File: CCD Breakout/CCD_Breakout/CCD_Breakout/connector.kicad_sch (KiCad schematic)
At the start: 2 parts

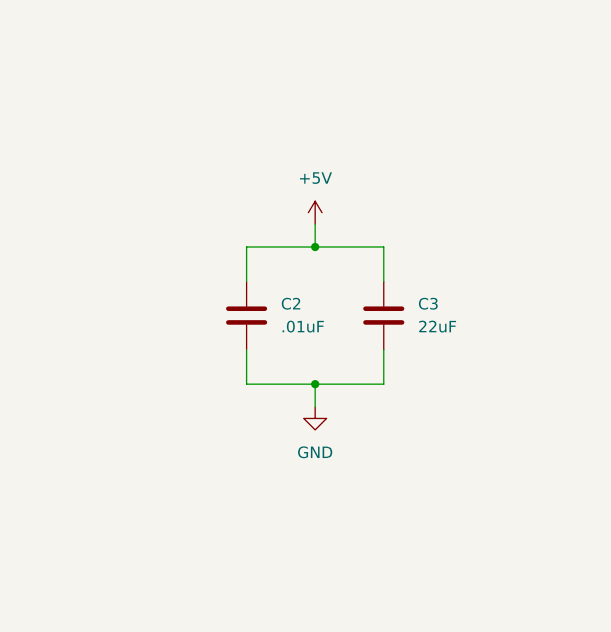
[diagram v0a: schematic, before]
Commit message: CCD Reorganization
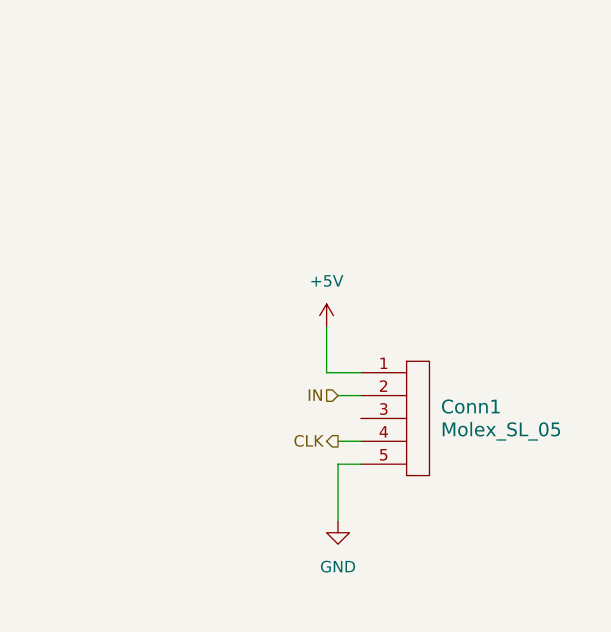
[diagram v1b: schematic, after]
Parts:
- removed C2: .01uF, symbol Device:C
- removed C3: 22uF, symbol Device:C
- added Conn1: Molex_SL_05, symbol MRDT_Connectors:Molex_SL_05
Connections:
- net +5V: now also Conn1.1
- net GND: now also Conn1.5
- new net CLK: Conn1.4
- new net IN: Conn1.2

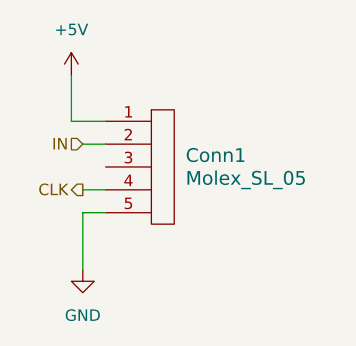
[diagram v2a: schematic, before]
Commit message: ADC Changes + Delete Fan Connector
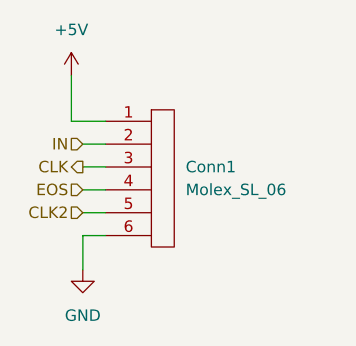
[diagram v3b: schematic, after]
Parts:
- removed Conn1: Molex_SL_05, symbol MRDT_Connectors:Molex_SL_05
- added Conn1: Molex_SL_06, symbol MRDT_Connectors:Molex_SL_06
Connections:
- net +5V: now also Conn1.1
- net CLK: now also Conn1.3
- net GND: now also Conn1.6
- net IN: now also Conn1.2
- new net CLK2: Conn1.5
- new net EOS: Conn1.4
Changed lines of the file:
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@@
+	(wire
+		(pts
+			(xy 149.86 97.79) (xy 152.4 97.79)
+		)
+		(stroke
+			(width 0)
+			(type default)
+		)
+	)
 	(wire
 		(pts
@@
 	(wire
 		(pts
-			(xy 149.86 97.79) (xy 152.4 97.79)
+			(xy 149.86 111.76) (xy 149.86 107.95)
 		)
 		(stroke
@@
 	(wire
 		(pts
-			(xy 149.86 111.76) (xy 149.86 105.41)
-		)
-		(stroke
-			(width 0)
-			(type default)
-		)
-	)
-	(wire
-		(pts
 			(xy 148.59 95.25) (xy 148.59 90.17)
 		)
@@
 	(wire
 		(pts
+			(xy 149.86 107.95) (xy 152.4 107.95)
+		)
+		(stroke
+			(width 0)
+			(type default)
+		)
+	)
+	(wire
+		(pts
 			(xy 152.4 95.25) (xy 148.59 95.25)
+		)
+		(stroke
+			(width 0)
+			(type default)
+		)
+	)
+	(wire
+		(pts
+			(xy 149.86 100.33) (xy 152.4 100.33)
 		)
 		(stroke
@@
 		)
 	)
-	(hierarchical_label "CLK"
-		(shape output)
+	(hierarchical_label "EOS"
+		(shape input)
 		(at 149.86 102.87 180)
 		(effects
@@
 		)
 	)
-	(symbol
-		(lib_id "MRDT_Connectors:Molex_SL_05")
-		(at 157.48 106.68 0)
-		(unit 1)
-		(exclude_from_sim no)
-		(in_bom yes)
-		(on_board yes)
-		(dnp no)
-		(fields_autoplaced yes)
-		(property "Reference" "Conn1"
-			(at 161.29 99.0599 0)
-			(effects
-				(font
-					(size 1.524 1.524)
-				)
-				(justify left)
-			)
-		)
-		(property "Value" "Molex_SL_05"
-			(at 161.29 101.5999 0)
-			(effects
-				(font
-					(size 1.524 1.524)
-				)
-				(justify left)
-			)
-		)
-		(property "Footprint" ""
-			(at 157.48 106.68 0)
-			(effects
-				(font
-					(size 1.524 1.524)
-				)
-				(hide yes)
-			)
-		)
-		(property "Datasheet" ""
-			(at 157.48 106.68 0)
-			(effects
-				(font
-					(size 1.524 1.524)
-				)
-				(hide yes)
-			)
-		)
-		(property "Description" ""
-			(at 157.48 106.68 0)
-			(effects
-				(font
-					(size 1.27 1.27)
-				)
-				(hide yes)
-			)
-		)
-		(pin "2"
-		)
-		(pin "1"
-		)
-		(pin "3"
-		)
-		(pin "5"
-		)
-		(pin "4"
-		)
-		(instances
-			(project ""
-				(path "/102965ac-29c6-4f96-94a4-d07431f6d693/dbede1ef-0855-4322-ae3b-1b9092ecc0c1"
-					(reference "Conn1")
-					(unit 1)
-				)
-			)
+	(hierarchical_label "CLK2"
+		(shape input)
+		(at 149.86 105.41 180)
+		(effects
+			(font
+				(size 1.27 1.27)
+			)
+			(justify right)
+		)
+	)
+	(hierarchical_label "CLK"
+		(shape output)
+		(at 149.86 100.33 180)
+		(effects
+			(font
+				(size 1.27 1.27)
+			)
+			(justify right)
 		)
 	)
@@
 					(unit 1)
 				)
+			)
+		)
+	)
+	(symbol
+		(lib_id "MRDT_Connectors:Molex_SL_06")
+		(at 157.48 109.22 0)
+		(unit 1)
+		(exclude_from_sim no)
+		(in_bom yes)
+		(on_board yes)
+		(dnp no)
+		(fields_autoplaced yes)
+		(property "Reference" "Conn1"
+			(at 161.29 100.3299 0)
+			(effects
+				(font
+					(size 1.27 1.27)
+				)
+				(justify left)
+			)
+		)
+		(property "Value" "Molex_SL_06"
+			(at 161.29 102.8699 0)
+			(effects
+				(font
+					(size 1.27 1.27)
+				)
+				(justify left)
+			)
+		)
+		(property "Footprint" ""
+			(at 152.4 105.41 0)
+			(effects
+				(font
+					(size 1.27 1.27)
+				)
+				(hide yes)
+			)
+		)
+		(property "Datasheet" ""
+			(at 152.4 105.41 0)
+			(effects
+				(font
+					(size 1.27 1.27)
+				)
+				(hide yes)
+			)
+		)
+		(property "Description" ""
+			(at 152.4 105.41 0)
+			(effects
+				(font
+					(size 1.27 1.27)
+				)
+				(hide yes)
+			)
+		)
+		(pin "1"
+		)
+		(pin "3"
+		)
+		(pin "5"
+		)
+		(pin "2"
+		)
+		(pin "4"
+		)
+		(pin "6"
+		)
+		(instances
+			(project ""
+				(path "/102965ac-29c6-4f96-94a4-d07431f6d693/dbede1ef-0855-4322-ae3b-1b9092ecc0c1"
+					(reference "Conn1")
+					(unit 1)
+				)

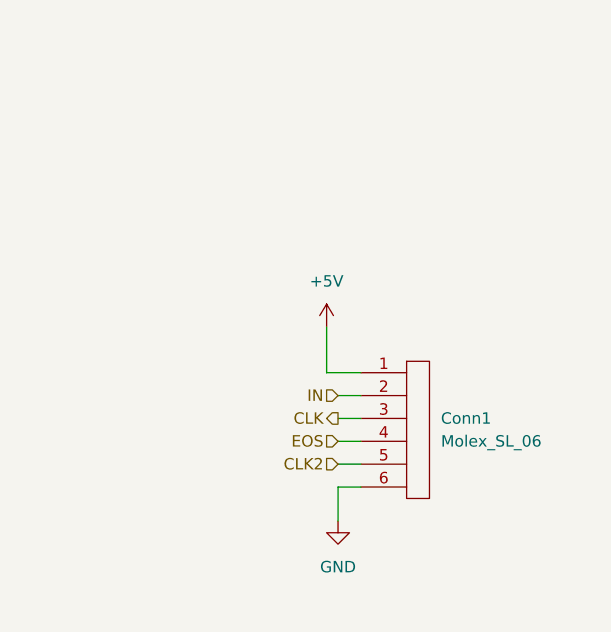
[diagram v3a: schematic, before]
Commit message: Removed Unnecessary Filtering Capacitors
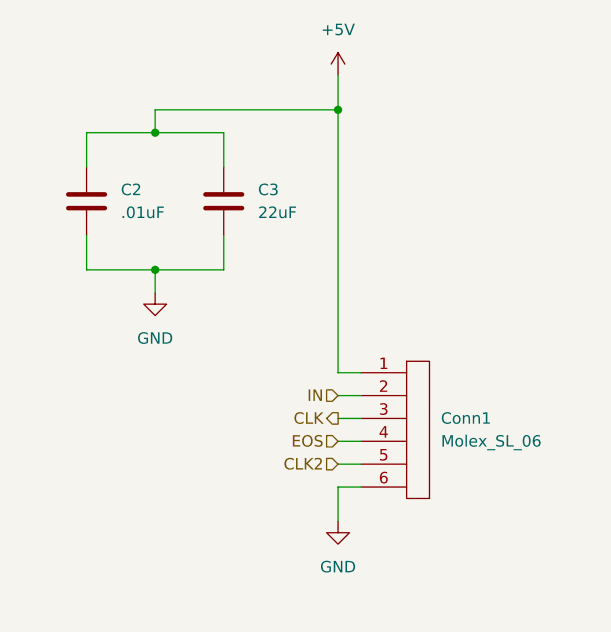
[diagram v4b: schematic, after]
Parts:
- added C2: .01uF, symbol Device:C
- added C3: 22uF, symbol Device:C
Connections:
- net +5V: now also C2.1, C3.1
- net GND: now also C2.2, C3.2

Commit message: ST and EOS Pin Connections
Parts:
- removed Conn1: Molex_SL_06, symbol MRDT_Connectors:Molex_SL_06
- added Conn1: Molex_SL_07, symbol MRDT_Connectors:Molex_SL_07
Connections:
- net +5V: now also Conn1.1
- net CLK: now also Conn1.3
- net CLK2: now also Conn1.6
- net EOS: now also Conn1.4
- net GND: now also Conn1.7
- net IN: now also Conn1.2
- new net ST: Conn1.5
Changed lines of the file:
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@@
+	(wire
+		(pts
+			(xy 152.4 110.49) (xy 149.86 110.49)
+		)
+		(stroke
+			(width 0)
+			(type default)
+		)
+	)
 	(wire
 		(pts
@@
 	(wire
 		(pts
+			(xy 149.86 110.49) (xy 149.86 115.57)
+		)
+		(stroke
+			(width 0)
+			(type default)
+		)
+	)
+	(wire
+		(pts
+			(xy 149.86 102.87) (xy 152.4 102.87)
+		)
+		(stroke
+			(width 0)
+			(type default)
+		)
+	)
+	(wire
+		(pts
+			(xy 149.86 62.23) (xy 149.86 66.04)
+		)
+		(stroke
+			(width 0)
+			(type default)
+		)
+	)
+	(wire
+		(pts
+			(xy 129.54 66.04) (xy 149.86 66.04)
+		)
+		(stroke
+			(width 0)
+			(type default)
+		)
+	)
+	(wire
+		(pts
+			(xy 152.4 95.25) (xy 149.86 95.25)
+		)
+		(stroke
+			(width 0)
+			(type default)
+		)
+	)
+	(wire
+		(pts
+			(xy 121.92 83.82) (xy 129.54 83.82)
+		)
+		(stroke
+			(width 0)
+			(type default)
+		)
+	)
+	(wire
+		(pts
+			(xy 149.86 107.95) (xy 152.4 107.95)
+		)
+		(stroke
+			(width 0)
+			(type default)
+		)
+	)
+	(wire
+		(pts
+			(xy 149.86 100.33) (xy 152.4 100.33)
+		)
+		(stroke
+			(width 0)
+			(type default)
+		)
+	)
+	(wire
+		(pts
+			(xy 121.92 80.01) (xy 121.92 83.82)
+		)
+		(stroke
+			(width 0)
+			(type default)
+		)
+	)
+	(wire
+		(pts
+			(xy 137.16 80.01) (xy 137.16 83.82)
+		)
+		(stroke
+			(width 0)
+			(type default)
+		)
+	)
+	(wire
+		(pts
 			(xy 149.86 105.41) (xy 152.4 105.41)
-		)
-		(stroke
-			(width 0)
-			(type default)
-		)
-	)
-	(wire
-		(pts
-			(xy 149.86 111.76) (xy 149.86 107.95)
-		)
-		(stroke
-			(width 0)
-			(type default)
-		)
-	)
-	(wire
-		(pts
-			(xy 149.86 102.87) (xy 152.4 102.87)
-		)
-		(stroke
-			(width 0)
-			(type default)
-		)
-	)
-	(wire
-		(pts
-			(xy 149.86 62.23) (xy 149.86 66.04)
-		)
-		(stroke
-			(width 0)
-			(type default)
-		)
-	)
-	(wire
-		(pts
-			(xy 129.54 66.04) (xy 149.86 66.04)
-		)
-		(stroke
-			(width 0)
-			(type default)
-		)
-	)
-	(wire
-		(pts
-			(xy 149.86 107.95) (xy 152.4 107.95)
-		)
-		(stroke
-			(width 0)
-			(type default)
-		)
-	)
-	(wire
-		(pts
-			(xy 152.4 95.25) (xy 149.86 95.25)
-		)
-		(stroke
-			(width 0)
-			(type default)
-		)
-	)
-	(wire
-		(pts
-			(xy 121.92 83.82) (xy 129.54 83.82)
-		)
-		(stroke
-			(width 0)
-			(type default)
-		)
-	)
-	(wire
-		(pts
-			(xy 149.86 100.33) (xy 152.4 100.33)
-		)
-		(stroke
-			(width 0)
-			(type default)
-		)
-	)
-	(wire
-		(pts
-			(xy 121.92 80.01) (xy 121.92 83.82)
-		)
-		(stroke
-			(width 0)
-			(type default)
-		)
-	)
-	(wire
-		(pts
-			(xy 137.16 80.01) (xy 137.16 83.82)
 		)
 		(stroke
@@
 		)
 	)
+	(hierarchical_label "ST"
+		(shape output)
+		(at 149.86 105.41 180)
+		(effects
+			(font
+				(size 1.27 1.27)
+			)
+			(justify right)
+		)
+	)
 	(hierarchical_label "EOS"
 		(shape input)
@@
 	(hierarchical_label "CLK2"
 		(shape input)
-		(at 149.86 105.41 180)
+		(at 149.86 107.95 180)
 		(effects
 			(font
@@
 	(symbol
 		(lib_id "power:GND")
-		(at 149.86 111.76 0)
+		(at 149.86 115.57 0)
 		(unit 1)
 		(exclude_from_sim no)
@@
 		(fields_autoplaced yes)
 		(property "Reference" "#PWR09"
-			(at 149.86 118.11 0)
+			(at 149.86 121.92 0)
 			(effects
 				(font
@@
 		)
 		(property "Value" "GND"
-			(at 149.86 116.84 0)
+			(at 149.86 120.65 0)
 			(effects
 				(font
@@
 		)
 		(property "Footprint" ""
-			(at 149.86 111.76 0)
+			(at 149.86 115.57 0)
 			(effects
 				(font
@@
 		)
 		(property "Datasheet" ""
-			(at 149.86 111.76 0)
+			(at 149.86 115.57 0)
 			(effects
 				(font
@@
 		)
 		(property "Description" "Power symbol creates a global label with name \"GND\" , ground"
-			(at 149.86 111.76 0)
+			(at 149.86 115.57 0)
 			(effects
 				(font
@@
 	)
 	(symbol
-		(lib_id "MRDT_Connectors:Molex_SL_06")
-		(at 157.48 109.22 0)
-		(unit 1)
-		(exclude_from_sim no)
-		(in_bom yes)
-		(on_board yes)
-		(dnp no)
-		(fields_autoplaced yes)
-		(property "Reference" "Conn1"
-			(at 161.29 100.3299 0)
-			(effects
-				(font
-					(size 1.27 1.27)
-				)
-				(justify left)
-			)
-		)
-		(property "Value" "Molex_SL_06"
-			(at 161.29 102.8699 0)
-			(effects
-				(font
-					(size 1.27 1.27)
-				)
-				(justify left)
-			)
-		)
-		(property "Footprint" ""
-			(at 152.4 105.41 0)
-			(effects
-				(font
-					(size 1.27 1.27)
-				)
-				(hide yes)
-			)
-		)
-		(property "Datasheet" ""
-			(at 152.4 105.41 0)
-			(effects
-				(font
-					(size 1.27 1.27)
-				)
-				(hide yes)
-			)
-		)
-		(property "Description" ""
-			(at 152.4 105.41 0)
-			(effects
-				(font
-					(size 1.27 1.27)
-				)
-				(hide yes)
-			)
-		)
-		(pin "1"
-		)
-		(pin "3"
-		)
-		(pin "5"
-		)
-		(pin "2"
-		)
-		(pin "4"
-		)
-		(pin "6"
-		)
-		(instances
-			(project ""
-				(path "/102965ac-29c6-4f96-94a4-d07431f6d693/dbede1ef-0855-4322-ae3b-1b9092ecc0c1"
-					(reference "Conn1")
-					(unit 1)
-				)
-			)
-		)
-	)
-	(symbol
 		(lib_id "power:GND")
 		(at 129.54 86.36 0)
@@
 					(unit 1)
 				)
+			)
+		)
+	)
+	(symbol
+		(lib_id "MRDT_Connectors:Molex_SL_07")
+		(at 157.48 111.76 0)
+		(unit 1)
+		(exclude_from_sim no)
+		(in_bom yes)
+		(on_board yes)
+		(dnp no)
+		(fields_autoplaced yes)
+		(property "Reference" "Conn1"
+			(at 161.29 101.5999 0)
+			(effects
+				(font
+					(size 1.524 1.524)
+				)
+				(justify left)
+			)
+		)
+		(property "Value" "Molex_SL_07"
+			(at 161.29 104.1399 0)
+			(effects
+				(font
+					(size 1.524 1.524)
+				)
+				(justify left)
+			)
+		)
+		(property "Footprint" ""
+			(at 157.48 106.68 0)
+			(effects
+				(font
+					(size 1.524 1.524)
+				)
+				(hide yes)
+			)
+		)
+		(property "Datasheet" ""
+			(at 157.48 106.68 0)
+			(effects
+				(font
+					(size 1.524 1.524)
+				)
+				(hide yes)
+			)
+		)
+		(property "Description" ""
+			(at 157.48 111.76 0)
+			(effects
+				(font
+					(size 1.27 1.27)
+				)
+				(hide yes)
+			)
+		)
+		(pin "5"
+		)
+		(pin "1"
+		)
+		(pin "3"
+		)
+		(pin "2"
+		)
+		(pin "4"
+		)
+		(pin "6"
+		)
+		(pin "7"
+		)
+		(instances
+			(project ""
+				(path "/102965ac-29c6-4f96-94a4-d07431f6d693/dbede1ef-0855-4322-ae3b-1b9092ecc0c1"
+					(reference "Conn1")
+					(unit 1)
+				)

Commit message: Fixed CCD Footprints
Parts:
- C2, C3: footprint (none) -> Capacitor_SMD:C_0603_1608Metric_Pad1.08x0.95mm_HandSolder
- Conn1: footprint (none) -> MRDT_Connectors:MOLEX_SL_07_Vertical
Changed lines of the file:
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@@
 			)
 		)
-		(property "Footprint" ""
+		(property "Footprint" "Capacitor_SMD:C_0603_1608Metric_Pad1.08x0.95mm_HandSolder"
 			(at 138.1252 80.01 0)
 			(effects
@@
 			)
 		)
-		(property "Footprint" ""
+		(property "Footprint" "MRDT_Connectors:MOLEX_SL_07_Vertical"
 			(at 157.48 106.68 0)
 			(effects
@@
 			)
 		)
-		(property "Footprint" ""
+		(property "Footprint" "Capacitor_SMD:C_0603_1608Metric_Pad1.08x0.95mm_HandSolder"
 			(at 122.8852 80.01 0)
 			(effects

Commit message: Added 3.3v to the CCD
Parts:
- removed Conn1: Molex_SL_07, MRDT_Connectors:MOLEX_SL_07_Vertical, symbol MRDT_Connectors:Molex_SL_07
- added Conn1: Molex_SL_08, symbol MRDT_Connectors:Molex_SL_08
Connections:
- net +5V: now also Conn1.2
- net CLK: now also Conn1.4
- net CLK2: now also Conn1.7
- net EOS: now also Conn1.5
- net GND: now also Conn1.8
- net IN: now also Conn1.3
- net ST: now also Conn1.6
- new net +3.3V: Conn1.1
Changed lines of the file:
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@@
 	(generator_version "9.0")
 	(paper "A4")
+	(text_box "Place this near to the connector"
+		(exclude_from_sim no)
+		(at 114.3 60.96 0)
+		(size 15.24 7.62)
+		(margins 0.9525 0.9525 0.9525 0.9525)
+		(stroke
+			(width 0)
+			(type solid)
+		)
+		(fill
+			(type none)
+		)
+		(effects
+			(font
+				(size 1.27 1.27)
+			)
+			(justify left top)
+		)
+	)
 	(junction
 		(at 149.86 66.04)
@@
 	(wire
 		(pts
+			(xy 147.32 92.71) (xy 152.4 92.71)
+		)
+		(stroke
+			(width 0)
+			(type default)
+		)
+	)
+	(wire
+		(pts
 			(xy 121.92 72.39) (xy 121.92 68.58)
 		)
@@
 		(pts
 			(xy 152.4 110.49) (xy 149.86 110.49)
+		)
+		(stroke
+			(width 0)
+			(type default)
+		)
+	)
+	(wire
+		(pts
+			(xy 147.32 87.63) (xy 147.32 92.71)
 		)
 		(stroke
@@
 	)
 	(symbol
+		(lib_id "power:+3.3V")
+		(at 147.32 87.63 0)
+		(unit 1)
+		(exclude_from_sim no)
+		(in_bom yes)
+		(on_board yes)
+		(dnp no)
+		(fields_autoplaced yes)
+		(property "Reference" "#PWR019"
+			(at 147.32 91.44 0)
+			(effects
+				(font
+					(size 1.27 1.27)
+				)
+				(hide yes)
+			)
+		)
+		(property "Value" "+3.3V"
+			(at 147.32 82.55 0)
+			(effects
+				(font
+					(size 1.27 1.27)
+				)
+			)
+		)
+		(property "Footprint" ""
+			(at 147.32 87.63 0)
+			(effects
+				(font
+					(size 1.27 1.27)
+				)
+				(hide yes)
+			)
+		)
+		(property "Datasheet" ""
+			(at 147.32 87.63 0)
+			(effects
+				(font
+					(size 1.27 1.27)
+				)
+				(hide yes)
+			)
+		)
+		(property "Description" "Power symbol creates a global label with name \"+3.3V\""
+			(at 147.32 87.63 0)
+			(effects
+				(font
+					(size 1.27 1.27)
+				)
+				(hide yes)
+			)
+		)
+		(pin "1"
+		)
+		(instances
+			(project ""
+				(path "/102965ac-29c6-4f96-94a4-d07431f6d693/dbede1ef-0855-4322-ae3b-1b9092ecc0c1"
+					(reference "#PWR019")
+					(unit 1)
+				)
+			)
+		)
+	)
+	(symbol
+		(lib_id "MRDT_Connectors:Molex_SL_08")
+		(at 157.48 111.76 0)
+		(unit 1)
+		(exclude_from_sim no)
+		(in_bom yes)
+		(on_board yes)
+		(dnp no)
+		(fields_autoplaced yes)
+		(property "Reference" "Conn1"
+			(at 161.29 100.3299 0)
+			(effects
+				(font
+					(size 1.524 1.524)
+				)
+				(justify left)
+			)
+		)
+		(property "Value" "Molex_SL_08"
+			(at 161.29 102.8699 0)
+			(effects
+				(font
+					(size 1.524 1.524)
+				)
+				(justify left)
+			)
+		)
+		(property "Footprint" ""
+			(at 157.48 104.14 0)
+			(effects
+				(font
+					(size 1.524 1.524)
+				)
+				(hide yes)
+			)
+		)
+		(property "Datasheet" ""
+			(at 157.48 104.14 0)
+			(effects
+				(font
+					(size 1.524 1.524)
+				)
+				(hide yes)
+			)
+		)
+		(property "Description" ""
+			(at 157.48 111.76 0)
+			(effects
+				(font
+					(size 1.27 1.27)
+				)
+				(hide yes)
+			)
+		)
+		(pin "2"
+		)
+		(pin "6"
+		)
+		(pin "5"
+		)
+		(pin "1"
+		)
+		(pin "8"
+		)
+		(pin "4"
+		)
+		(pin "7"
+		)
+		(pin "3"
+		)
+		(instances
+			(project ""
+				(path "/102965ac-29c6-4f96-94a4-d07431f6d693/dbede1ef-0855-4322-ae3b-1b9092ecc0c1"
+					(reference "Conn1")
+					(unit 1)
+				)
+			)
+		)
+	)
+	(symbol
 		(lib_id "power:GND")
 		(at 129.54 86.36 0)
@@
 					(unit 1)
 				)
-			)
-		)
-	)
-	(symbol
-		(lib_id "MRDT_Connectors:Molex_SL_07")
-		(at 157.48 111.76 0)
-		(unit 1)
-		(exclude_from_sim no)
-		(in_bom yes)
-		(on_board yes)
-		(dnp no)
-		(fields_autoplaced yes)
-		(property "Reference" "Conn1"
-			(at 161.29 101.5999 0)
-			(effects
-				(font
-					(size 1.524 1.524)
-				)
-				(justify left)
-			)
-		)
-		(property "Value" "Molex_SL_07"
-			(at 161.29 104.1399 0)
-			(effects
-				(font
-					(size 1.524 1.524)
-				)
-				(justify left)
-			)
-		)
-		(property "Footprint" "MRDT_Connectors:MOLEX_SL_07_Vertical"
-			(at 157.48 106.68 0)
-			(effects
-				(font
-					(size 1.524 1.524)
-				)
-				(hide yes)
-			)
-		)
-		(property "Datasheet" ""
-			(at 157.48 106.68 0)
-			(effects
-				(font
-					(size 1.524 1.524)
-				)
-				(hide yes)
-			)
-		)
-		(property "Description" ""
-			(at 157.48 111.76 0)
-			(effects
-				(font
-					(size 1.27 1.27)
-				)
-				(hide yes)
-			)
-		)
-		(pin "5"
-		)
-		(pin "1"
-		)
-		(pin "3"
-		)
-		(pin "2"
-		)
-		(pin "4"
-		)
-		(pin "6"
-		)
-		(pin "7"
-		)
-		(instances
-			(project ""
-				(path "/102965ac-29c6-4f96-94a4-d07431f6d693/dbede1ef-0855-4322-ae3b-1b9092ecc0c1"
-					(reference "Conn1")
-					(unit 1)
-				)

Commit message: Added 3.3v to ADC
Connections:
- net +3.3V renamed +3V3
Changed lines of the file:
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@@
+	)
+	(symbol
+		(lib_id "power:+3V3")
+		(at 147.32 87.63 0)
+		(unit 1)
+		(exclude_from_sim no)
+		(in_bom yes)
+		(on_board yes)
+		(dnp no)
+		(fields_autoplaced yes)
+		(property "Reference" "#PWR019"
+			(at 147.32 91.44 0)
+			(effects
+				(font
+					(size 1.27 1.27)
+				)
+				(hide yes)
+			)
+		)
+		(property "Value" "+3V3"
+			(at 147.32 82.55 0)
+			(effects
+				(font
+					(size 1.27 1.27)
+				)
+			)
+		)
+		(property "Footprint" ""
+			(at 147.32 87.63 0)
+			(effects
+				(font
+					(size 1.27 1.27)
+				)
+				(hide yes)
+			)
+		)
+		(property "Datasheet" ""
+			(at 147.32 87.63 0)
+			(effects
+				(font
+					(size 1.27 1.27)
+				)
+				(hide yes)
+			)
+		)
+		(property "Description" "Power symbol creates a global label with name \"+3V3\""
+			(at 147.32 87.63 0)
+			(effects
+				(font
+					(size 1.27 1.27)
+				)
+				(hide yes)
+			)
+		)
+		(pin "1"
+		)
+		(instances
+			(project ""
+				(path "/102965ac-29c6-4f96-94a4-d07431f6d693/dbede1ef-0855-4322-ae3b-1b9092ecc0c1"
+					(reference "#PWR019")
+					(unit 1)
+				)
+			)
+		)
 	)
 	(symbol
@@
 					(unit 1)
 				)
-			)
-		)
-	)
-	(symbol
-		(lib_id "power:+3.3V")
-		(at 147.32 87.63 0)
-		(unit 1)
-		(exclude_from_sim no)
-		(in_bom yes)
-		(on_board yes)
-		(dnp no)
-		(fields_autoplaced yes)
-		(property "Reference" "#PWR019"
-			(at 147.32 91.44 0)
-			(effects
-				(font
-					(size 1.27 1.27)
-				)
-				(hide yes)
-			)
-		)
-		(property "Value" "+3.3V"
-			(at 147.32 82.55 0)
-			(effects
-				(font
-					(size 1.27 1.27)
-				)
-			)
-		)
-		(property "Footprint" ""
-			(at 147.32 87.63 0)
-			(effects
-				(font
-					(size 1.27 1.27)
-				)
-				(hide yes)
-			)
-		)
-		(property "Datasheet" ""
-			(at 147.32 87.63 0)
-			(effects
-				(font
-					(size 1.27 1.27)
-				)
-				(hide yes)
-			)
-		)
-		(property "Description" "Power symbol creates a global label with name \"+3.3V\""
-			(at 147.32 87.63 0)
-			(effects
-				(font
-					(size 1.27 1.27)
-				)
-				(hide yes)
-			)
-		)
-		(pin "1"
-		)
-		(instances
-			(project ""
-				(path "/102965ac-29c6-4f96-94a4-d07431f6d693/dbede1ef-0855-4322-ae3b-1b9092ecc0c1"
-					(reference "#PWR019")
-					(unit 1)
-				)
